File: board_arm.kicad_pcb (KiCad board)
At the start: 2 copper layers, 314.3 x 95.2 mm, 151 parts, among them SW1 5.2x5.2mm, U1 ATmega32U4-AU, U2 PRTR5V0U2X, Y1 16MHz

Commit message: ARM board
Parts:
- removed F1: 500mA, Fuse:Fuse_1206_3216Metric
- removed R6: 5.1k, Resistor_SMD:R_0805_2012Metric
- removed Y1: 16MHz, Crystal:Crystal_SMD_3225-4Pin_3.2x2.5mm
- added C10: 1nF, Capacitor_SMD:C_0805_2012Metric, B.Cu at (378.1, 99.8)
- added C11: 10uF, Capacitor_SMD:C_0805_2012Metric, B.Cu at (381.4, 101.8)
- added C8: 1uF, Capacitor_SMD:C_0805_2012Metric, B.Cu at (377.1, 123.8)
- added C9: 10uF, Capacitor_SMD:C_0805_2012Metric, B.Cu at (387.4, 128.3)
- added SW2: SW_SPDT, Button_Switch_SMD:SW_SPST_SKQG_WithoutStem, B.Cu at (352.4, 116.7)
- added U3: MCP1725-3302E_SN, Package_QFP:LQFP-32_7x7mm_P0.8mm, B.Cu at (352.4, 130.2)
- C1, C2: value 22pF -> 0.1uF
- C3: value 1uF -> 0.1uF
- C5, C6: value 0.1uF -> 4.7uF
- C7: value 10uF -> 10nF
- R2: value 1k -> 10k
- R3: value 22 -> 10k
- R4: value 22 -> 5.1k
- SW1: value 5.2x5.2mm -> SW_Push
- U1: value ATmega32U4-AU -> STM32F072CBT6; footprint Package_QFP:TQFP-44_10x10mm_P0.8mm -> locallib:MCP1725-3302E_SN
- moved R4 50.3 mm to (384.8, 101.8), turned to 0 degrees
- moved R3 49.4 mm to (381.5, 99.8), turned to 0 degrees
- moved C6 46.3 mm to (381.4, 103.7), turned to 0 degrees
- moved R2 45.0 mm to (378.1, 97.9)
- moved R1 41.5 mm to (384.8, 103.7), turned to 0 degrees
- moved C7 39.2 mm to (374.7, 96.7), turned to 0 degrees
- moved C5 33.2 mm to (378.0, 101.8)
- moved C3 27.2 mm to (371.3, 96.7), turned to 0 degrees
- moved U1 24.7 mm to (337.3, 88.1)
- moved SW1 23.1 mm to (352.4, 107.2)
- moved C1 22.8 mm to (371.3, 98.7)
- moved C4 21.4 mm to (374.7, 98.7)
- moved C2 21.1 mm to (378.0, 103.7), turned to 0 degrees
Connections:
- C1 pad 1: Net-(C1-Pad1) -> +3V3
- C2 pad 1: Net-(C2-Pad1) -> +3V3
- C3 pad 1: Net-(C3-Pad1) -> +3V3
- C4 pad 1: +5V -> +3V3
- C5 pad 1: +5V -> +3V3
- C6 pad 1: +5V -> +3V3
- C7 pad 1: +5V -> +3V3
- R1 pad 1: +5V -> Net-(R1-Pad1)
- R2 pad 1: GND -> +5V
- R3 pad 1: D- -> PWRGD
- R3 pad 2: Net-(R3-Pad2) -> +3V3
- R4 pad 1: D+ -> GND
- SW1 pad 2: Net-(R1-Pad2) -> PWRGD
- U1 pad 1: Net-(U1-Pad1) -> +3V3
- U1 pad 2: +5V -> Net-(U1-Pad2)
- U1 pad 3: D- -> Net-(U1-Pad3)
- U1 pad 4: D+ -> Net-(U1-Pad4)
- U1 pad 5: GND -> Net-(U1-Pad5)
- U1 pad 6: Net-(C3-Pad1) -> Net-(U1-Pad6)
- U1 pad 7: +5V -> PWRGD
- U1 pad 8: Net-(U1-Pad8) -> GND
- U2 pad 2: Net-(R4-Pad2) -> D+
- U2 pad 3: Net-(R3-Pad2) -> D-
- U2 pad 4: VCC -> +5V
- USB1 pad 10: Net-(R6-Pad2) -> Net-(R5-Pad2)
- USB1 pad 11: VCC -> +5V
- USB1 pad 2: VCC -> +5V
- USB1 pad 4: Net-(R5-Pad2) -> Net-(R4-Pad2)
- USB1 pad 5: Net-(R3-Pad2) -> D-
- USB1 pad 6: Net-(R4-Pad2) -> D+
- USB1 pad 7: Net-(R3-Pad2) -> D-
- USB1 pad 8: Net-(R4-Pad2) -> D+
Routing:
- net VCC: track 19.5 -> 0.00 mm, vias 2 -> 0
- net +5V: track 0.00 -> 19.5 mm, vias 0 -> 2
- net Net-(R4-Pad2): track 13.3 -> 0.00 mm
- net D+: track 0.00 -> 13.3 mm
- net Net-(R3-Pad2): track 12.1 -> 0.00 mm
- net D-: track 0.00 -> 12.1 mm
- net Net-(R6-Pad2): track 7.74 -> 0.00 mm, vias 2 -> 0
- net Net-(R5-Pad2): track 13.3 -> 21.0 mm, vias 2 -> 4

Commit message: Fix MCU wires
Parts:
- SW1: footprint random-keyboard-parts:PushButton_6x6mm_TH -> Button_Switch_SMD:SW_SPST_SKQG_WithoutStem
- SW2: footprint Button_Switch_SMD:SW_SPST_SKQG_WithoutStem -> Button_Switch_SMD:SW_SPDT_PCM12
- U1: footprint locallib:MCP1725-3302E_SN -> Package_QFP:LQFP-48_7x7mm_P0.5mm
- U3: footprint Package_QFP:LQFP-32_7x7mm_P0.8mm -> locallib:MCP1725-3302E_SN
- moved U3 46.7 mm to (338.1, 85.7), turned to 270 degrees
- moved U1 44.7 mm to (352.4, 130.2), turned to 0 degrees

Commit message: Pretty
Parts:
- moved SW2 2.38 mm to (352.4, 114.3)
- moved SW1 0.79 mm to (352.4, 106.4)
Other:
- outline, holes or cut-outs redrawn

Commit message: Add switch footprint
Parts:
- SW2: footprint Button_Switch_SMD:SW_SPDT_PCM12 -> locallib:JS102011SCQN
- moved SW2 0.79 mm to (352.4, 115.1), turned to 90 degrees
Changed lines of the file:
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@@
     (add_net GND)
   )
+  (module locallib:JS102011SCQN (layer B.Cu)
+    (at 352.425 115.09375 90)
+    (fp_text reference SW2 (at -5.55625 0 180) (layer B.SilkS)
+      (effects (font (size 1 1) (thickness 0.15)) (justify mirror))
+    )
+    (fp_text value SW_SPDT (at 5.2 0 180) (layer B.Fab)
+      (effects (font (size 1 1) (thickness 0.15)) (justify mirror))
+    )
+    (fp_line (start 4.445 4.25) (end 4.445 -4.25) (layer B.CrtYd) (width 0.05))
+    (fp_line (start -4.445 -4.25) (end 4.445 -4.25) (layer B.CrtYd) (width 0.05))
+    (fp_line (start -4.445 4.25) (end -4.445 -4.25) (layer B.CrtYd) (width 0.05))
+    (fp_line (start -4.445 4.25) (end 4.445 4.25) (layer B.CrtYd) (width 0.05))
+    (fp_line (start -1.8 -0.8) (end -1.8 0.8) (layer B.SilkS) (width 0.12))
+    (fp_line (start -1.8 -0.8) (end 1.8 -0.8) (layer B.SilkS) (width 0.12))
+    (fp_line (start 1.8 0.8) (end 1.8 -0.8) (layer B.SilkS) (width 0.12))
+    (fp_line (start -1.8 0.8) (end 1.8 0.8) (layer B.SilkS) (width 0.12))
+    (fp_line (start -1.69 -1.86) (end 1.69 -1.86) (layer B.SilkS) (width 0.12))
+    (fp_line (start 3.31 -1.86) (end 4.36 -1.86) (layer B.SilkS) (width 0.12))
+    (fp_line (start 4.36 1.86) (end 4.36 -1.86) (layer B.SilkS) (width 0.12))
+    (fp_line (start -4.36 1.86) (end -4.36 -1.86) (layer B.SilkS) (width 0.12))
+    (fp_line (start -4.36 -1.86) (end -3.31 -1.86) (layer B.SilkS) (width 0.12))
+    (fp_line (start -4.36 1.86) (end -0.81 1.86) (layer B.SilkS) (width 0.12))
+    (fp_line (start -4.25 1.75) (end -4.25 -1.75) (layer B.Fab) (width 0.1))
+    (fp_line (start 4.25 -1.75) (end -4.25 -1.75) (layer B.Fab) (width 0.1))
+    (fp_line (start 4.25 1.75) (end 4.25 -1.75) (layer B.Fab) (width 0.1))
+    (fp_line (start -4.25 1.75) (end 4.25 1.75) (layer B.Fab) (width 0.1))
+    (fp_line (start 0.81 1.86) (end 4.36 1.86) (layer B.SilkS) (width 0.12))
+    (fp_line (start -4.25 1.75) (end -4.25 -1.75) (layer B.Fab) (width 0.1))
+    (fp_line (start 4.25 -1.75) (end -4.25 -1.75) (layer B.Fab) (width 0.1))
+    (fp_line (start 4.25 1.75) (end 4.25 -1.75) (layer B.Fab) (width 0.1))
+    (pad 3 smd rect (at 2.5 -2.75 90) (size 1 2.5) (layers B.Cu B.Paste B.Mask)
+      (net 98 +3V3))
+    (pad 2 smd rect (at 0 2.75 90) (size 1 2.5) (layers B.Cu B.Paste B.Mask)
+      (net 90 "Net-(R1-Pad2)"))
+    (pad 1 smd rect (at -2.5 -2.75 90) (size 1 2.5) (layers B.Cu B.Paste B.Mask)
+      (net 1 GND))
+  )
   (module Button_Switch_SMD:SW_SPST_SKQG_WithoutStem (layer B.Cu)
     (at 352.425 106.3625)
@@
       (net 2 +5V))
   )
-  (module Button_Switch_SMD:SW_SPDT_PCM12 (layer B.Cu)
-    (at 352.425 114.3)
-    (descr "Ultraminiature Surface Mount Slide Switch")
-    (attr smd)
-    (fp_text reference SW2 (at 0 3.2) (layer B.SilkS)
-      (effects (font (size 1 1) (thickness 0.15)) (justify mirror))
-    )
-    (fp_text value SW_SPDT (at 0 -4.25) (layer B.Fab)
-      (effects (font (size 1 1) (thickness 0.15)) (justify mirror))
-    )
-    (fp_text user %R (at 0 3.2) (layer B.Fab)
-      (effects (font (size 1 1) (thickness 0.15)) (justify mirror))
-    )
-    (fp_line (start -1.4 -1.65) (end -1.4 -2.95) (layer B.Fab) (width 0.1))
-    (fp_line (start -1.4 -2.95) (end -1.2 -3.15) (layer B.Fab) (width 0.1))
-    (fp_line (start -1.2 -3.15) (end -0.35 -3.15) (layer B.Fab) (width 0.1))
-    (fp_line (start -0.35 -3.15) (end -0.15 -2.95) (layer B.Fab) (width 0.1))
-    (fp_line (start -0.15 -2.95) (end -0.1 -2.9) (layer B.Fab) (width 0.1))
-    (fp_line (start -0.1 -2.9) (end -0.1 -1.6) (layer B.Fab) (width 0.1))
-    (fp_line (start -3.35 1) (end -3.35 -1.6) (layer B.Fab) (width 0.1))
-    (fp_line (start -3.35 -1.6) (end 3.35 -1.6) (layer B.Fab) (width 0.1))
-    (fp_line (start 3.35 -1.6) (end 3.35 1) (layer B.Fab) (width 0.1))
-    (fp_line (start 3.35 1) (end -3.35 1) (layer B.Fab) (width 0.1))
-    (fp_line (start 1.4 1.12) (end 1.6 1.12) (layer B.SilkS) (width 0.12))
-    (fp_line (start -4.4 2.45) (end 4.4 2.45) (layer B.CrtYd) (width 0.05))
-    (fp_line (start 4.4 2.45) (end 4.4 -2.1) (layer B.CrtYd) (width 0.05))
-    (fp_line (start 4.4 -2.1) (end 1.65 -2.1) (layer B.CrtYd) (width 0.05))
-    (fp_line (start 1.65 -2.1) (end 1.65 -3.4) (layer B.CrtYd) (width 0.05))
-    (fp_line (start 1.65 -3.4) (end -1.65 -3.4) (layer B.CrtYd) (width 0.05))
-    (fp_line (start -1.65 -3.4) (end -1.65 -2.1) (layer B.CrtYd) (width 0.05))
-    (fp_line (start -1.65 -2.1) (end -4.4 -2.1) (layer B.CrtYd) (width 0.05))
-    (fp_line (start -4.4 -2.1) (end -4.4 2.45) (layer B.CrtYd) (width 0.05))
-    (fp_line (start -1.4 -3.02) (end -1.2 -3.23) (layer B.SilkS) (width 0.12))
-    (fp_line (start -0.1 -3.02) (end -0.3 -3.23) (layer B.SilkS) (width 0.12))
-    (fp_line (start -1.4 -1.73) (end -1.4 -3.02) (layer B.SilkS) (width 0.12))
-    (fp_line (start -1.2 -3.23) (end -0.3 -3.23) (layer B.SilkS) (width 0.12))
-    (fp_line (start -0.1 -3.02) (end -0.1 -1.73) (layer B.SilkS) (width 0.12))
-    (fp_line (start -2.85 -1.73) (end 2.85 -1.73) (layer B.SilkS) (width 0.12))
-    (fp_line (start -1.6 1.12) (end 0.1 1.12) (layer B.SilkS) (width 0.12))
-    (fp_line (start -3.45 0.07) (end -3.45 -0.72) (layer B.SilkS) (width 0.12))
-    (fp_line (start 3.45 -0.72) (end 3.45 0.07) (layer B.SilkS) (width 0.12))
-    (pad "" np_thru_hole circle (at -1.5 -0.33) (size 0.9 0.9) (drill 0.9) (layers *.Cu *.Mask))
-    (pad "" np_thru_hole circle (at 1.5 -0.33) (size 0.9 0.9) (drill 0.9) (layers *.Cu *.Mask))
-    (pad 1 smd rect (at -2.25 1.43) (size 0.7 1.5) (layers B.Cu B.Paste B.Mask)
-      (net 1 GND))
-    (pad 2 smd rect (at 0.75 1.43) (size 0.7 1.5) (layers B.Cu B.Paste B.Mask)
-      (net 90 "Net-(R1-Pad2)"))
-    (pad 3 smd rect (at 2.25 1.43) (size 0.7 1.5) (layers B.Cu B.Paste B.Mask)
-      (net 98 +3V3))
-    (pad "" smd rect (at -3.65 -1.43) (size 1 0.8) (layers B.Cu B.Paste B.Mask))
-    (pad "" smd rect (at 3.65 -1.43) (size 1 0.8) (layers B.Cu B.Paste B.Mask))
-    (pad "" smd rect (at 3.65 0.78) (size 1 0.8) (layers B.Cu B.Paste B.Mask))
-    (pad "" smd rect (at -3.65 0.78) (size 1 0.8) (layers B.Cu B.Paste B.Mask))
-    (model ${KISYS3DMOD}/Button_Switch_SMD.3dshapes/SW_SPDT_PCM12.wrl
-      (at (xyz 0 0 0))
-      (scale (xyz 1 1 1))
-      (rotate (xyz 0 0 0))
-    )
-  )
   (module Package_QFP:LQFP-48_7x7mm_P0.5mm (layer B.Cu)

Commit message: More fixes
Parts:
- removed SW2: SW_SPDT, locallib:JS102011SCQN
- SW1: value SW_Push -> SW_SPDT; footprint Button_Switch_SMD:SW_SPST_SKQG_WithoutStem -> locallib:SW_SPDT_9.0x3.5mm
- moved SW1 3.64 mm to (352.5, 110.0)
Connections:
- SW1 pad 2: PWRGD -> Net-(R1-Pad2)

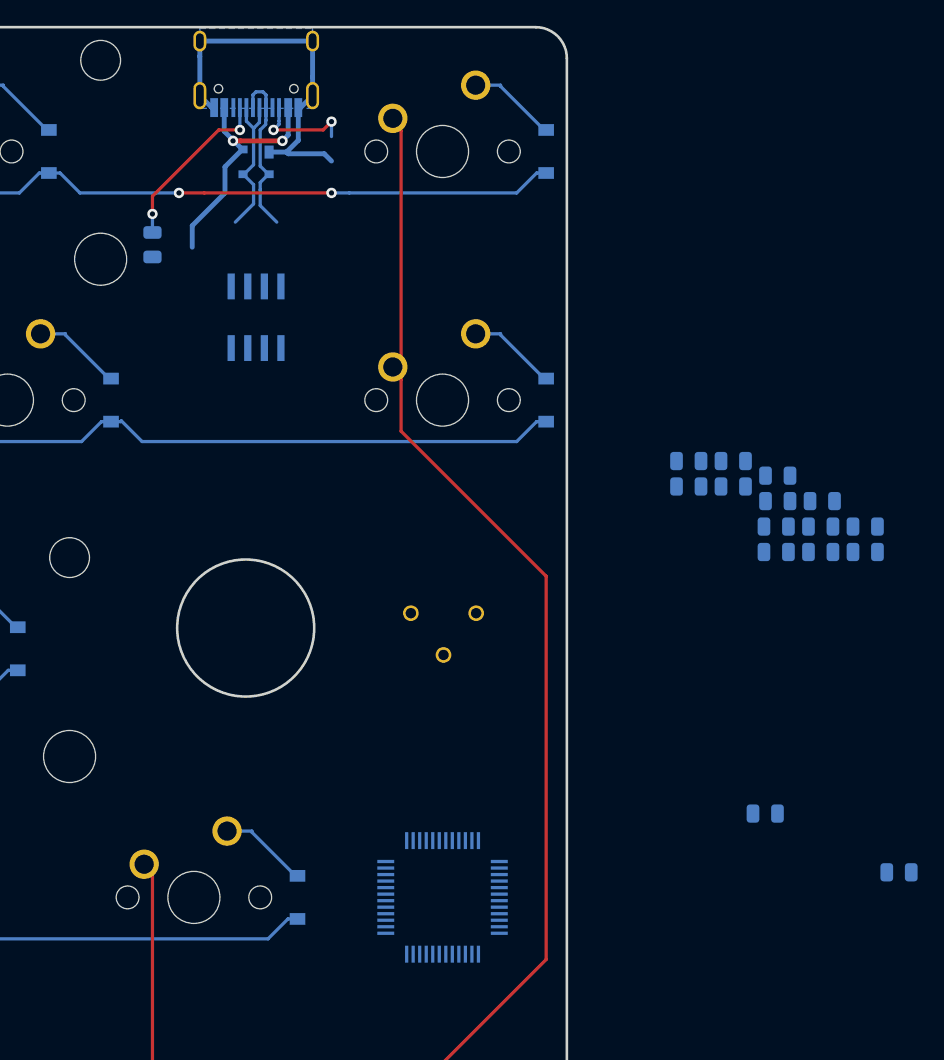
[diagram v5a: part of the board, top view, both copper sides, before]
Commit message: rerouting of the USB and reg
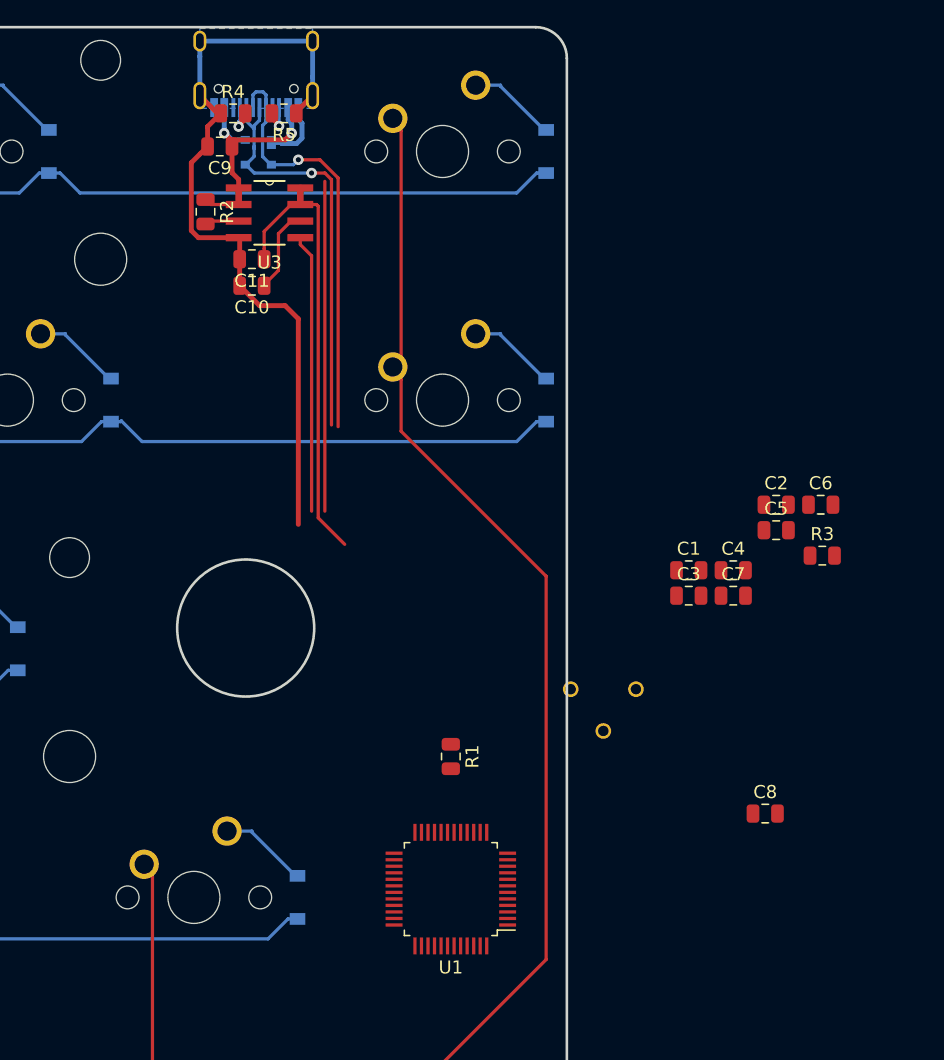
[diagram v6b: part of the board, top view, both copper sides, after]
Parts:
- C1, C10, C11, C2, C3, C4, C5, C6, C7, C8, C9, R1, R2, R3, R4, R5, U1, U3: moved to F.Cu
- moved C9 76.2 mm to (335.4, 72.6), turned to 180 degrees
- moved R4 57.9 mm to (336.4, 70.1)
- moved R2 48.3 mm to (334.3, 77.6), turned to 270 degrees
- moved C11 48.2 mm to (337.8, 81.3), turned to 180 degrees
- moved C10 43.5 mm to (337.8, 83.3), turned to 180 degrees
- moved R1 35.4 mm to (353.1, 119.4), turned to 270 degrees
- moved R5 14.2 mm to (340.3, 70.1), turned to 180 degrees
- moved SW1 13.6 mm to (364.7, 115.8)
- moved C3 10.3 mm to (371.3, 107.1)
- moved C7 10.3 mm to (374.7, 107.1)
- moved U3 8.07 mm to (339.2, 77.7), turned to 0 degrees
- moved C1 6.42 mm to (371.3, 105.1)
- moved C4 6.42 mm to (374.7, 105.1)
- moved R3 4.18 mm to (381.5, 104.0)
- moved C2 3.62 mm to (378.0, 100.1)
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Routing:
- net GND: track 28.8 -> 93.1 mm
- net +3V3: track 0.00 -> 35.2 mm
- net PWRGD: track 0.00 -> 21.3 mm
- net D-: track 12.1 -> 32.7 mm, vias 0 -> 1
- net D+: track 13.3 -> 32.8 mm, vias 0 -> 1
- net Net-(R5-Pad2): track 21.0 -> 2.61 mm, vias 4 -> 1
- net Net-(C10-Pad1): track 0.00 -> 6.55 mm
- net Net-(R4-Pad2): track 0.00 -> 2.72 mm, vias 0 -> 1
- net Net-(R2-Pad2): track 0.00 -> 2.63 mm
- net +5V: track 19.5 -> 18.3 mm
- net ROW0: vias 2 -> 0
